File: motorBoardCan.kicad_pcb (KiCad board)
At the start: 6 copper layers, 50 x 50 mm, 75 parts, among them J1 Conn_01x04_Pin, J10 Conn_01x02_Pin, J11 Conn_01x02_Pin, J12 Conn_01x02_Pin, J2 Conn_01x04_Pin, J3 Conn_02x04_Top_Bottom, J4 Conn_01x02_Pin, J5 Conn_01x02_Pin, J6 Conn_02x04_Top_Bottom, J7 Conn_01x02_Pin, J8 Conn_01x02_Pin, J9 Conn_01x02_Pin, Q1 AO3400A, Q2 AO3400A, Q3 AO3400A, Q4 AO3400A, U1 NUCLEO-G431KB, U10 TPS563200, U4 SN65HVD230, U5 LD1117S33TR_SOT223

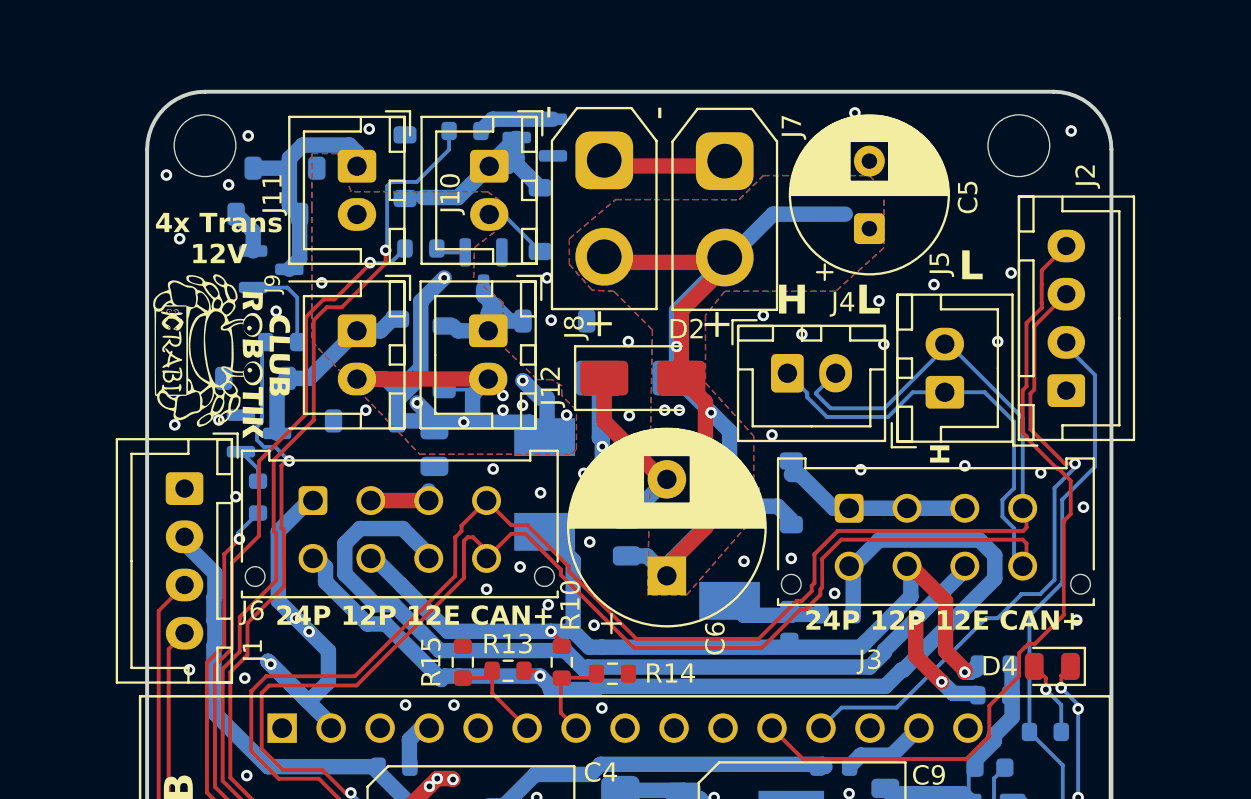
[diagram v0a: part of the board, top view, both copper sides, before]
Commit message: update to Kicad 10 + fix warnings
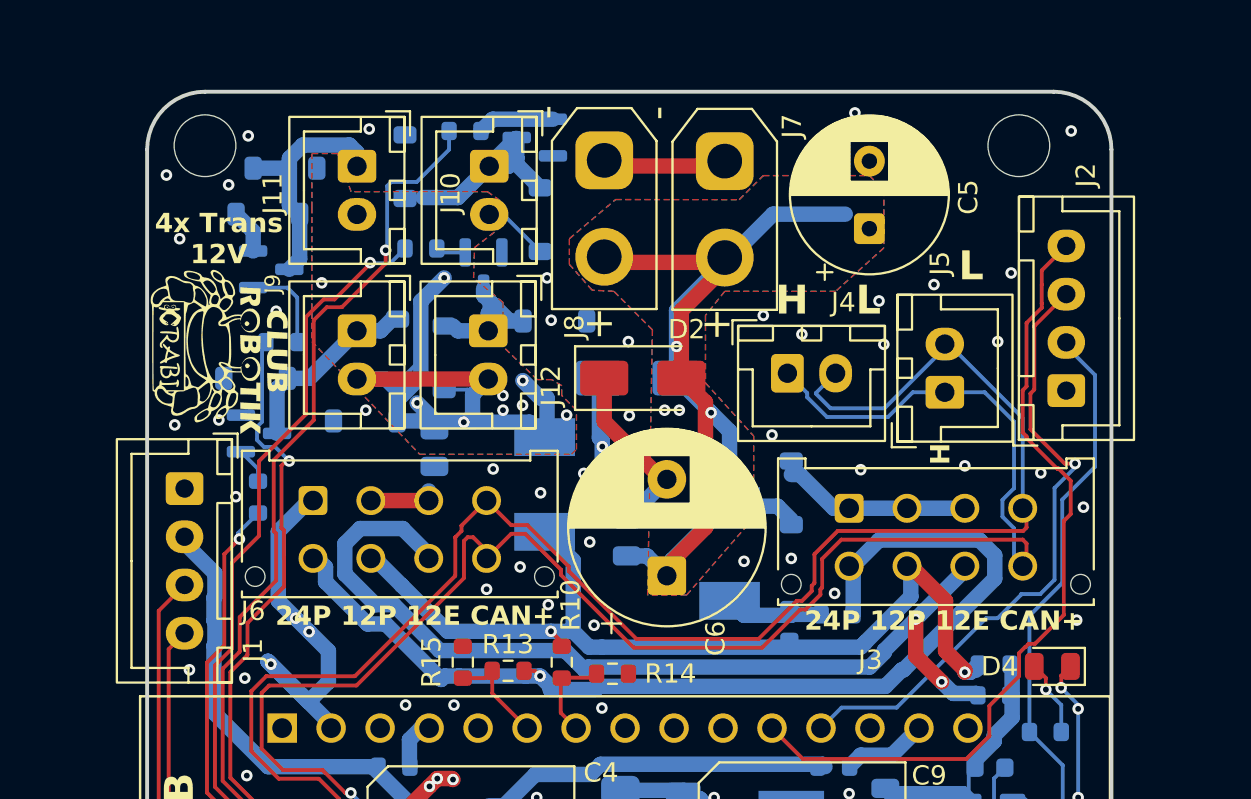
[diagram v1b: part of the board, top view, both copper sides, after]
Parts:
- moved G*** 0.26 mm to (80.6, 70.9)

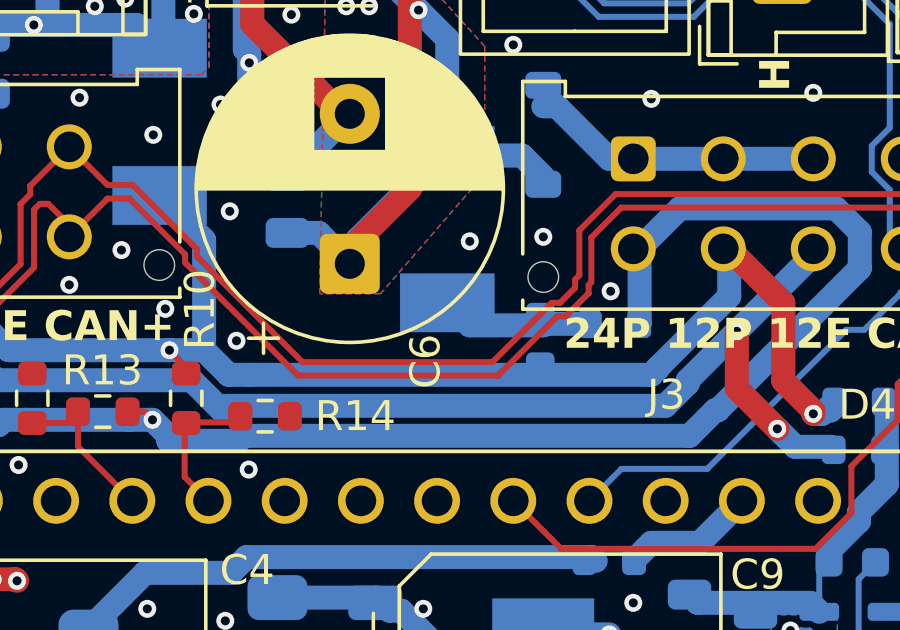
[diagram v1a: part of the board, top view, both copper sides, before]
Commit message: bigger jumper resistors
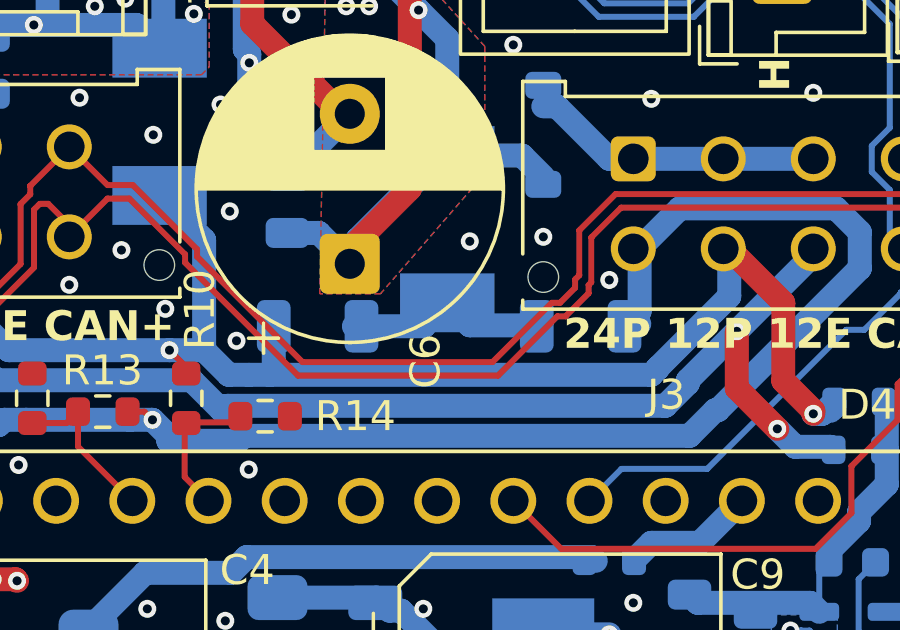
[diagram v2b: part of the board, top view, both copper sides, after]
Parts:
- R11, R12: footprint Resistor_SMD:R_0603_1608Metric -> Resistor_SMD:R_1206_3216Metric
- moved R12 7.44 mm to (102.7, 84.6), turned to 180 degrees
- moved R11 1.13 mm to (111.4, 84.6)
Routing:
- net 12V_POW_P: track 53.9 -> 55.6 mm
- net Net-(F1-Pad2): track 5.51 -> 7.17 mm
- net 24V_POW_P: track 62.2 -> 63.0 mm

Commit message: improve GND routing
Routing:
- net GND: vias 77 -> 84
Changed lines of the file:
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@@
 	)
 	(via
+		(at 101.854 82.804)
+		(size 0.6)
+		(drill 0.3)
+		(layers "F.Cu" "B.Cu")
+		(free yes)
+		(net "GND")
+	)
+	(via
 		(at 88.138 73.914)
 		(size 0.6)
@@
 	)
 	(via
+		(at 125.984 70.866)
+		(size 0.6)
+		(drill 0.3)
+		(layers "F.Cu" "B.Cu")
+		(free yes)
+		(net "GND")
+	)
+	(via
 		(at 84.5 84.7)
 		(size 0.6)
@@
 	)
 	(via
+		(at 95.758 62.738)
+		(size 0.6)
+		(drill 0.3)
+		(layers "F.Cu" "B.Cu")
+		(free yes)
+		(net "GND")
+	)
+	(via
 		(at 101.4 101.6)
 		(size 0.6)
@@
 	)
 	(via
+		(at 83.312 64.516)
+		(size 0.6)
+		(drill 0.3)
+		(layers "F.Cu" "B.Cu")
+		(free yes)
+		(net "GND")
+	)
+	(via
 		(at 118.2 98.05)
 		(size 0.6)
@@
 	)
 	(via
+		(at 93.218 58.42)
+		(size 0.6)
+		(drill 0.3)
+		(layers "F.Cu" "B.Cu")
+		(free yes)
+		(net "GND")
+	)
+	(via
 		(at 125.075 94)
 		(size 0.6)
@@
 	)
 	(via
+		(at 94.488 80.01)
+		(size 0.6)
+		(drill 0.3)
+		(layers "F.Cu" "B.Cu")
+		(free yes)
+		(net "GND")
+	)
+	(via
 		(at 83.4898 68.7832)
 		(size 0.6)
@@
 	)
 	(via
+		(at 96.52 88.9)
+		(size 0.6)
+		(drill 0.3)
+		(layers "F.Cu" "B.Cu")
+		(free yes)
+		(net "GND")
+	)
+	(via
 		(at 80.518 96.52)
 		(size 0.6)
@@
 	)
 	(segment
+		(start 104 98.85)
+		(end 104 98.95)
+		(width 0.8)
+		(layer "B.Cu")
+		(net "5V")
+	)
+	(segment
 		(start 105.7 100.65)
 		(end 104 98.95)
@@
 	)
 	(segment
-		(start 102.065 98.95)
-		(end 104 98.95)
-		(width 0.8)
-		(layer "B.Cu")
-		(net "5V")
-	)
-	(segment
 		(start 114.6 100.65)
 		(end 115.2 100.05)
@@
 	)
 	(segment
-		(start 101.34 98.225)
-		(end 102.065 98.95)
-		(width 0.8)
-		(layer "B.Cu")
-		(net "5V")
-	)
-	(segment
 		(start 110.475 100.65)
 		(end 114.6 100.65)
@@
 	)
 	(segment
+		(start 103.375 98.225)
+		(end 104 98.85)
+		(width 0.8)
+		(layer "B.Cu")
+		(net "5V")
+	)
+	(segment
 		(start 101.34 98.225)
 		(end 101.14 98.425)
@@
 		(layer "B.Cu")
 		(net "5V")
+	)
+	(segment
+		(start 101.34 98.225)
+		(end 103.375 98.225)
+		(width 0.8)
+		(layer "B.Cu")
+		(net "5V")
